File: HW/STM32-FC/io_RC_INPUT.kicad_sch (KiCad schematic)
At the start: 5 parts, among them J2 DSM, J4 RCIN, Q1 S9013

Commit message: 250102:STM32F407VET
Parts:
- added J9: RCIN, PWM_Connector:PWM_Conn_3x02, symbol PWM_Connector:PWM_Conn_3x01
- J4: symbol PWM_Connector:PWM_Conn_3x02 -> PWM_Connector:PWM_Conn_3x01
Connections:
- net +5V: now also J4.2 (5V), J9.2 (5V); no longer J4.3 (5V)
- net GND: now also J4.3 (GND), J9.3 (GND); no longer J4.4 (GND)
- net RSSI_IN: no longer J4.2 (CH2)
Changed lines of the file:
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@@
 		(color 0 0 0 0)
 	)
-	(junction
-		(at 49.53 48.26)
-		(diameter 0)
-		(color 0 0 0 0)
-	)
 	(wire
 		(pts
@@
 	(wire
 		(pts
+			(xy -20.32 60.96) (xy -11.43 60.96)
+		)
+		(stroke
+			(width 0)
+			(type default)
+		)
+	)
+	(wire
+		(pts
 			(xy 76.2 40.64) (xy 86.36 40.64)
 		)
@@
 	(wire
 		(pts
-			(xy 48.26 50.8) (xy 57.15 50.8)
-		)
-		(stroke
-			(width 0)
-			(type default)
-		)
-	)
-	(wire
-		(pts
 			(xy 55.88 105.41) (xy 54.61 105.41)
 		)
@@
 	(wire
 		(pts
-			(xy 49.53 63.5) (xy 52.07 63.5)
-		)
-		(stroke
-			(width 0)
-			(type default)
-		)
-	)
-	(wire
-		(pts
-			(xy 48.26 48.26) (xy 49.53 48.26)
-		)
-		(stroke
-			(width 0)
-			(type default)
-		)
-	)
-	(wire
-		(pts
 			(xy 76.2 38.1) (xy 76.2 40.64)
 		)
@@
 	(wire
 		(pts
+			(xy -36.83 54.61) (xy -35.56 54.61)
+		)
+		(stroke
+			(width 0)
+			(type default)
+		)
+	)
+	(wire
+		(pts
 			(xy 76.2 31.75) (xy 76.2 33.02)
 		)
@@
 	(wire
 		(pts
-			(xy 49.53 48.26) (xy 62.23 48.26)
-		)
-		(stroke
-			(width 0)
-			(type default)
-		)
-	)
-	(wire
-		(pts
-			(xy 49.53 48.26) (xy 49.53 63.5)
+			(xy -36.83 49.53) (xy -35.56 49.53)
+		)
+		(stroke
+			(width 0)
+			(type default)
+		)
+	)
+	(wire
+		(pts
+			(xy 48.26 48.26) (xy 62.23 48.26)
 		)
 		(stroke
@@
 		)
 	)
+	(label "RSSI_IN"
+		(at -11.43 60.96 180)
+		(fields_autoplaced yes)
+		(effects
+			(font
+				(size 1 1)
+			)
+			(justify right bottom)
+		)
+	)
 	(label "UART1_RX"
 		(at 60.96 139.7 180)
@@
 	(label "UART1_RX"
 		(at 63.5 110.49 180)
-		(fields_autoplaced yes)
-		(effects
-			(font
-				(size 1 1)
-			)
-			(justify right bottom)
-		)
-	)
-	(label "RSSI_IN"
-		(at 57.15 50.8 180)
 		(fields_autoplaced yes)
 		(effects
@@
 	)
 	(symbol
+		(lib_id "PWM_Connector:PWM_Conn_3x01")
+		(at -27.94 52.07 0)
+		(mirror y)
+		(unit 1)
+		(exclude_from_sim no)
+		(in_bom yes)
+		(on_board yes)
+		(dnp no)
+		(property "Reference" "J9"
+			(at -27.94 44.196 0)
+			(effects
+				(font
+					(size 1 1)
+				)
+			)
+		)
+		(property "Value" "RCIN"
+			(at -27.94 45.974 0)
+			(effects
+				(font
+					(size 1 1)
+				)
+			)
+		)
+		(property "Footprint" "PWM_Connector:PWM_Conn_3x02"
+			(at -36.83 55.88 0)
+			(effects
+				(font
+					(size 1.27 1.27)
+				)
+				(hide yes)
+			)
+		)
+		(property "Datasheet" "~"
+			(at -36.83 55.88 0)
+			(effects
+				(font
+					(size 1.27 1.27)
+				)
+				(hide yes)
+			)
+		)
+		(property "Description" "Generic connector, single row, 01x03, script generated (kicad-library-utils/schlib/autogen/connector/)"
+			(at -27.94 55.88 0)
+			(effects
+				(font
+					(size 1.27 1.27)
+				)
+				(hide yes)
+			)
+		)
+		(pin "1"
+		)
+		(pin "2"
+		)
+		(pin "3"
+		)
+		(instances
+			(project "STM32-FC"
+				(path "/8d4cc317-3933-4aa6-844b-8c5c635e89c7/77caf73d-b7f5-48a6-9de3-ef3df69ee7d9"
+					(reference "J9")
+					(unit 1)
+				)
+			)
+		)
+	)
+	(symbol
 		(lib_id "power:+3.3V")
 		(at 55.88 102.87 0)
@@
 	)
 	(symbol
+		(lib_id "power:+5V")
+		(at -36.83 49.53 90)
+		(unit 1)
+		(exclude_from_sim no)
+		(in_bom yes)
+		(on_board yes)
+		(dnp no)
+		(property "Reference" "#PWR059"
+			(at -33.02 49.53 0)
+			(effects
+				(font
+					(size 1.27 1.27)
+				)
+				(hide yes)
+			)
+		)
+		(property "Value" "+5V"
+			(at -38.354 47.752 90)
+			(effects
+				(font
+					(size 1 1)
+				)
+			)
+		)
+		(property "Footprint" ""
+			(at -36.83 49.53 0)
+			(effects
+				(font
+					(size 1.27 1.27)
+				)
+				(hide yes)
+			)
+		)
+		(property "Datasheet" ""
+			(at -36.83 49.53 0)
+			(effects
+				(font
+					(size 1.27 1.27)
+				)
+				(hide yes)
+			)
+		)
+		(property "Description" ""
+			(at -36.83 49.53 0)
+			(effects
+				(font
+					(size 1.27 1.27)
+				)
+				(hide yes)
+			)
+		)
+		(pin "1"
+		)
+		(instances
+			(project "STM32-FC"
+				(path "/8d4cc317-3933-4aa6-844b-8c5c635e89c7/77caf73d-b7f5-48a6-9de3-ef3df69ee7d9"
+					(reference "#PWR059")
+					(unit 1)
+				)
+			)
+		)
+	)
+	(symbol
+		(lib_id "power:GND")
+		(at -36.83 54.61 270)
+		(unit 1)
+		(exclude_from_sim no)
+		(in_bom yes)
+		(on_board yes)
+		(dnp no)
+		(property "Reference" "#PWR060"
+			(at -43.18 54.61 0)
+			(effects
+				(font
+					(size 1.27 1.27)
+				)
+				(hide yes)
+			)
+		)
+		(property "Value" "GND"
+			(at -38.1 57.15 90)
+			(effects
+				(font
+					(size 1 1)
+				)
+			)
+		)
+		(property "Footprint" ""
+			(at -36.83 54.61 0)
+			(effects
+				(font
+					(size 1.27 1.27)
+				)
+				(hide yes)
+			)
+		)
+		(property "Datasheet" ""
+			(at -36.83 54.61 0)
+			(effects
+				(font
+					(size 1.27 1.27)
+				)
+				(hide yes)
+			)
+		)
+		(property "Description" ""
+			(at -36.83 54.61 0)
+			(effects
+				(font
+					(size 1.27 1.27)
+				)
+				(hide yes)
+			)
+		)
+		(pin "1"
+		)
+		(instances
+			(project "STM32-FC"
+				(path "/8d4cc317-3933-4aa6-844b-8c5c635e89c7/77caf73d-b7f5-48a6-9de3-ef3df69ee7d9"
+					(reference "#PWR060")
+					(unit 1)
+				)
+			)
+		)
+	)
+	(symbol
 		(lib_id "power:GND")
 		(at 58.42 105.41 180)
@@
 	)
 	(symbol
-		(lib_id "PWM_Connector:PWM_Conn_3x02")
+		(lib_id "PWM_Connector:PWM_Conn_3x01")
 		(at 40.64 50.8 0)
 		(mirror y)
@@
 		(pin "3"
 		)
-		(pin "4"
-		)
-		(instances
+		(instances

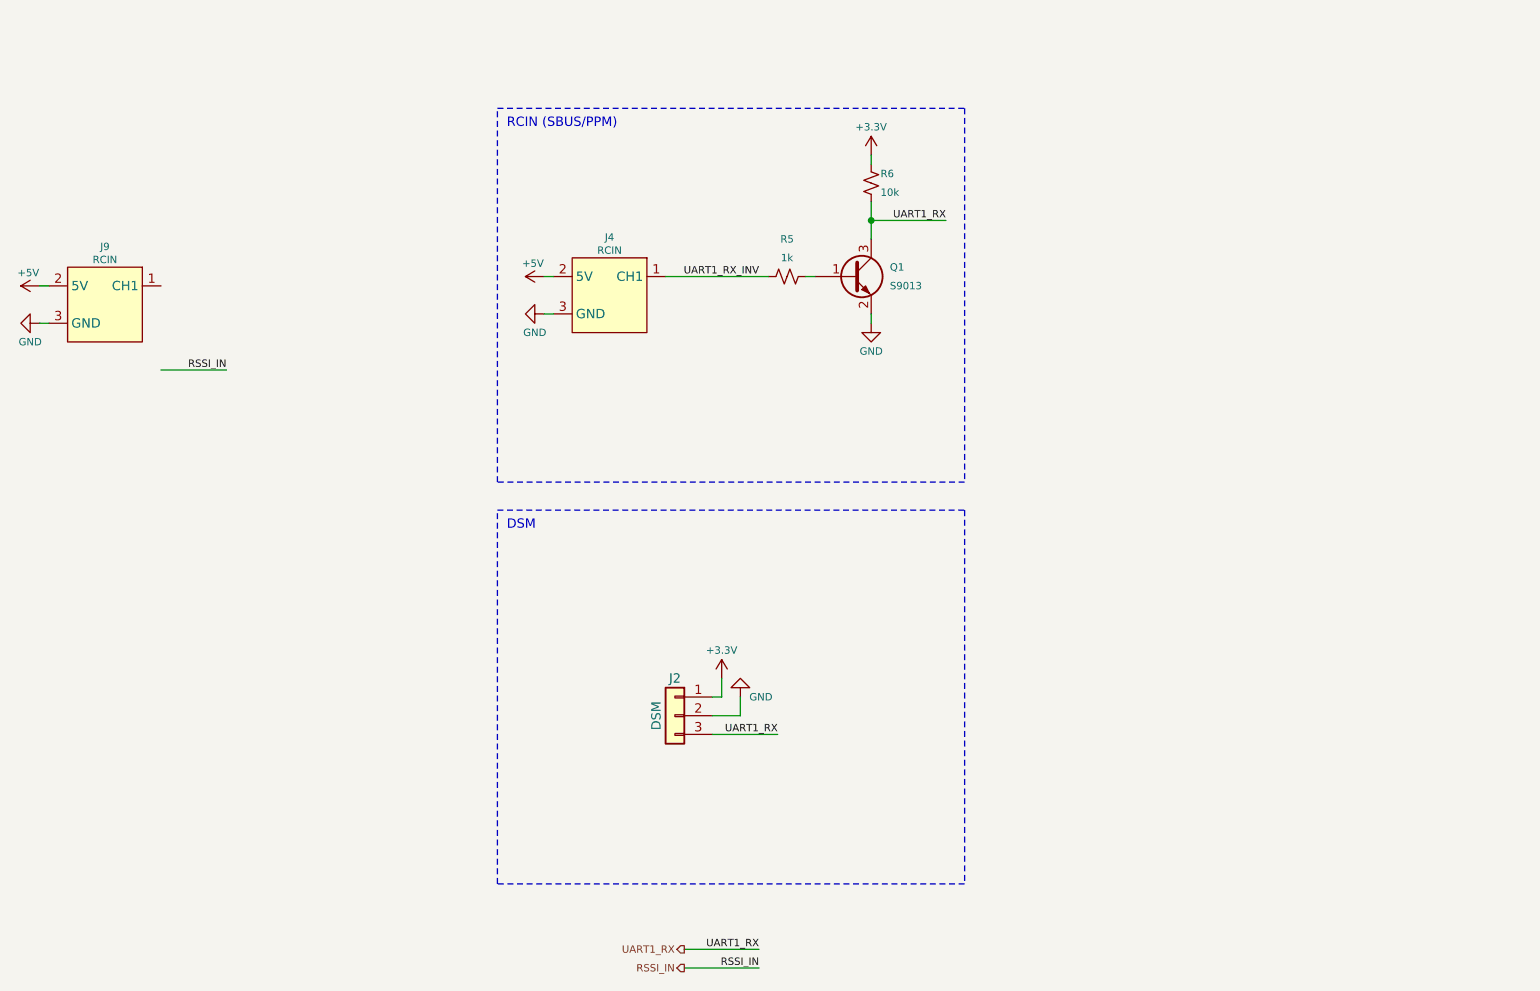
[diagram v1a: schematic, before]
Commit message: RC IN modified
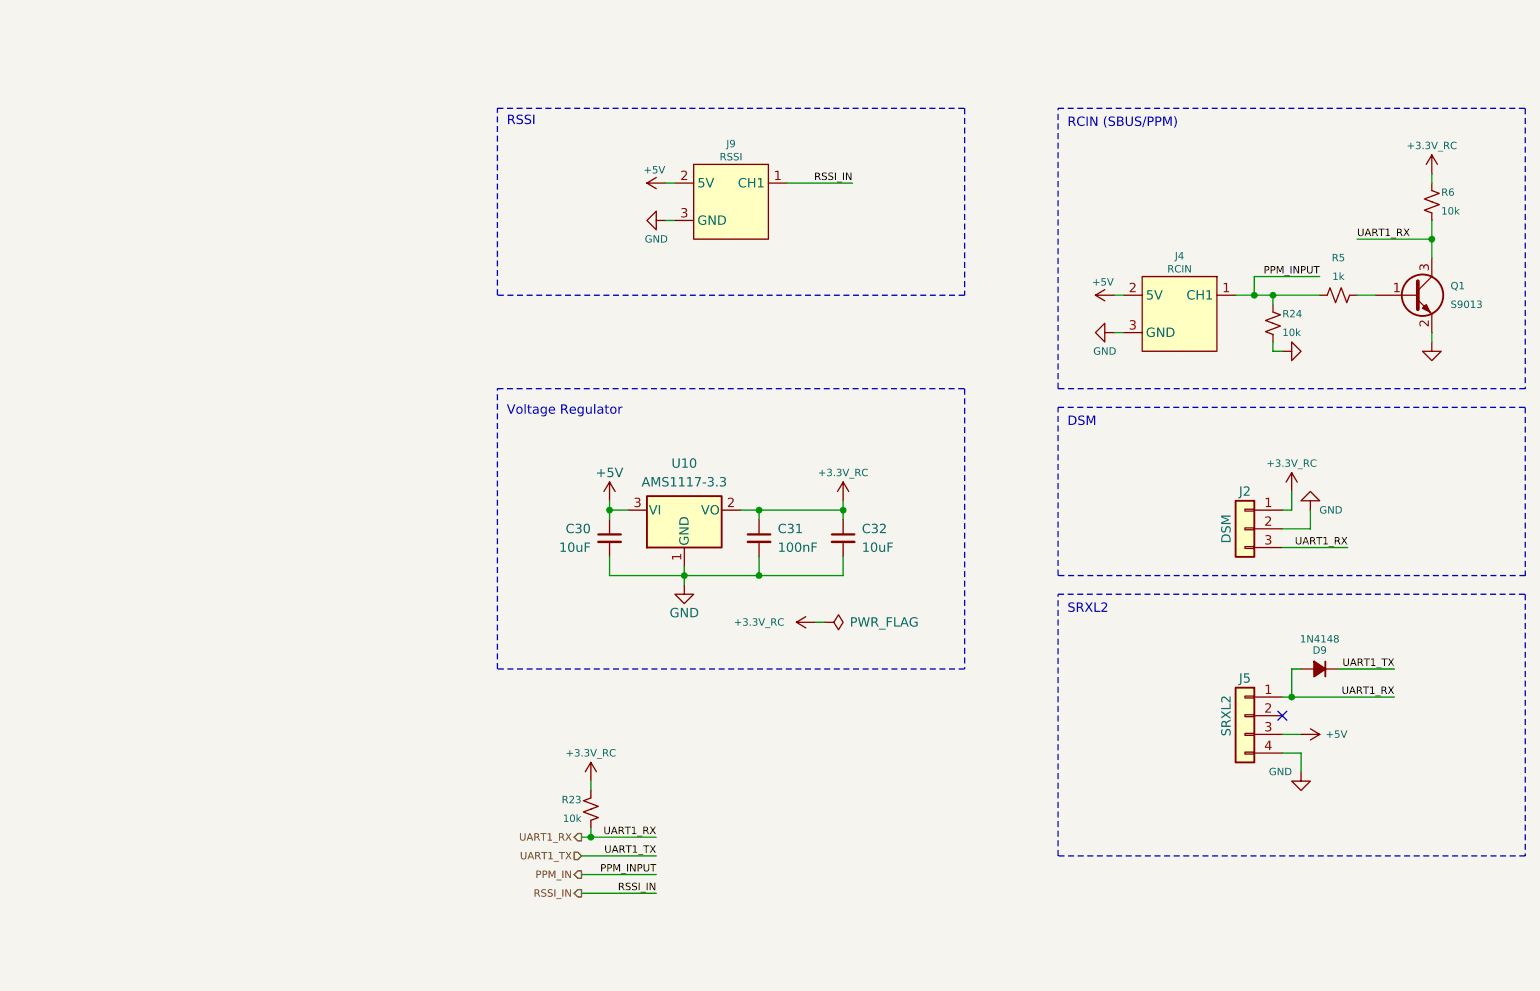
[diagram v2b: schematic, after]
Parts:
- added C30, C32: 10uF, Capacitor_SMD:C_0402_1005Metric, symbol Device:C_Small
- added C31: 100nF, Capacitor_SMD:C_0402_1005Metric, symbol Device:C_Small
- added D9: 1N4148, symbol Device:D_Small_Filled
- added J5: SRXL2, Connector_JST:JST_ZH_B3B-ZR-SM4-TF_1x03-1MP_P1.50mm_Vertical, symbol Connector_Generic:Conn_01x04
- added R23, R24: 10k, Resistor_SMD:R_0402_1005Metric, symbol Device:R_Small_US
- added U10: AMS1117-3.3, Package_TO_SOT_SMD:SOT-223-3_TabPin2, symbol Regulator_Linear:AMS1117-3.3
- J2: footprint Connector_PinHeader_2.54mm:PinHeader_1x03_P2.54mm_Vertical -> Connector_JST:JST_ZH_B3B-ZR-SM4-TF_1x03-1MP_P1.50mm_Vertical
- J9: value RCIN -> RSSI
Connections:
- net +5V: now also C30.1, J5.3 (Pin_3), U10.3 (VI)
- net GND: now also C30.2, C31.2, C32.2, J5.4 (Pin_4), R24.2, U10.1 (GND)
- net RSSI_IN: now also J9.1 (CH1)
- net UART1_RX: now also D9.2 (A), J5.1 (Pin_1), R23.2
- net +3.3V renamed +3.3V_RC
- net +3.3V_RC: now also C31.1, C32.1, R23.1, U10.2 (VO)
- net UART1_RX_INV renamed PPM_IN
- net PPM_IN: now also R24.1
- new net UART1_TX: D9.1 (K)
- no-connect marks 0 -> 1
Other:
- note added: "RSSI"
- note added: "SRXL2"
- note added: "Voltage Regulator"
- moved on the sheet: J2, J4, J9, Q1, R5, R6

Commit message: Big Update:IMU/RC/Conn./MCU
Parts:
- removed C30, C32: 10uF, Capacitor_SMD:C_0402_1005Metric, symbol Device:C_Small
- removed C31: 100nF, Capacitor_SMD:C_0402_1005Metric, symbol Device:C_Small
- removed U10: AMS1117-3.3, Package_TO_SOT_SMD:SOT-223-3_TabPin2, symbol Regulator_Linear:AMS1117-3.3
- D8: renamed from D9; footprint (none) -> Diode_SMD:D_SOD-123
- J7: renamed from J5; footprint Connector_JST:JST_ZH_B3B-ZR-SM4-TF_1x03-1MP_P1.50mm_Vertical -> Connector_JST:JST_ZH_B4B-ZR-SM4-TF_1x04-1MP_P1.50mm_Vertical
- Q2: renamed from Q1; footprint digikey-footprints:SOT-23-3 -> Package_TO_SOT_SMD:SOT-23-3
- renumbered J4 to J5, J2 to J6, J9 to J8, R24 to R12, R5 to R13, R6 to R14, R23 to R15
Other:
- note added: "2.54mm 3P PC0 : RSSI_IN"
- note added: "2.54mm 3P SBUS - PA10 : UART1_RX PPM - PB7 : TIM4_CH2"
- note added: "ZH 1.5mm 3P PA10 : UART1_RX"
- note added: "ZH 1.5mm 4P PA9 : UART1_TX PA10 : UART1_RX"
- note removed: "Voltage Regulator"
- company: (none) -> INHA UNIV. NARAE
- title: (none) -> RC_INPUT
- moved on the sheet: D8, J5, J6, J7, J8, Q2, R12, R13, R14, R15

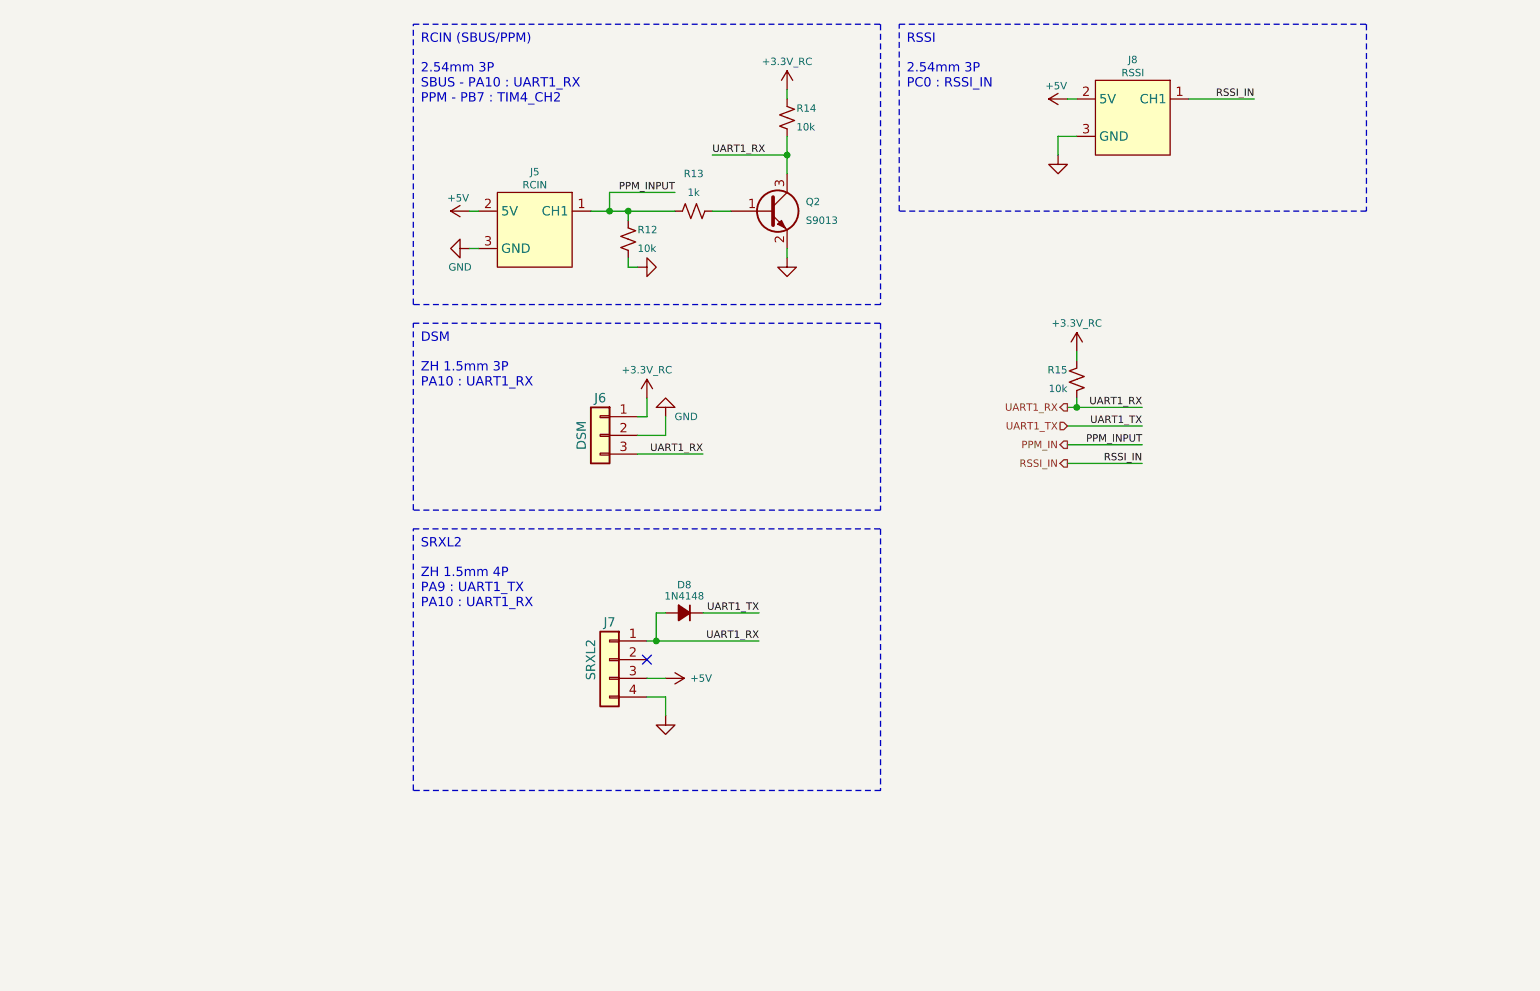
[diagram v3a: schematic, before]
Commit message: 2025.01.03v2:PM(Power Module) added
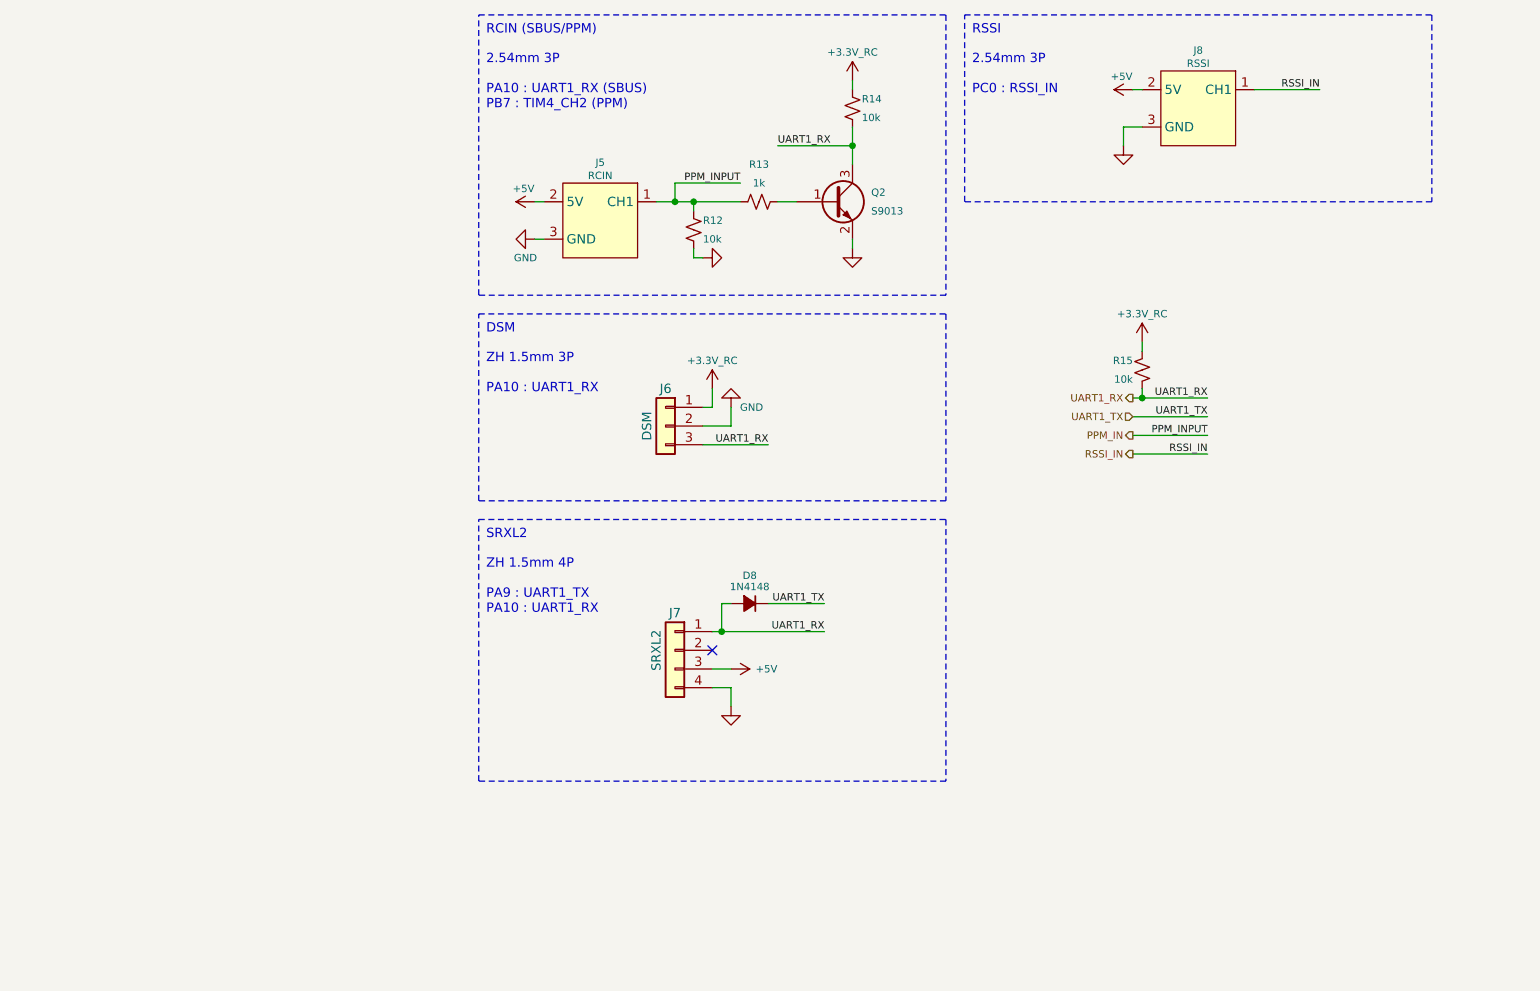
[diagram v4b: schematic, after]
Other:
- note added: "2.54mm 3P PA10 : UART1_RX (SBUS) PB7 : TIM4_CH2 (PPM)"
- note removed: "2.54mm 3P SBUS - PA10 : UART1_RX PPM - PB7 : TIM4_CH2"
- company: INHA UNIV. NARAE -> NARAE
- moved on the sheet: D8, J5, J6, J7, J8, Q2, R12, R13, R14, R15

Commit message: Baro/SD Card update
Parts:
- removed J5: RCIN, PWM_Connector:PWM_Conn_3x02, symbol PWM_Connector:PWM_Conn_3x01
- added J11: PWM_Conn_3x01, PWM_Connector:PWM_Conn_3x01, symbol PWM_Connector:PWM_Conn_3x01
- J10: renamed from J7; value SRXL2 -> ZH 1.5mm 4P; footprint Connector_JST:JST_ZH_B4B-ZR-SM4-TF_1x04-1MP_P1.50mm_Vertical -> Connector_JST:JST_ZH_S4B-ZR-SM4A-TF_1x04-1MP_P1.50mm_Horizontal
- J8: value RSSI -> PWM_Conn_3x01; footprint PWM_Connector:PWM_Conn_3x02 -> PWM_Connector:PWM_Conn_3x01
- J9: renamed from J6; value DSM -> ZH 1.5mm 3P; footprint Connector_JST:JST_ZH_B3B-ZR-SM4-TF_1x03-1MP_P1.50mm_Vertical -> Connector_JST:JST_ZH_S3B-ZR-SM4A-TF_1x03-1MP_P1.50mm_Horizontal
- renumbered D8 to D7, R12 to R18, R13 to R19, R14 to R20, R15 to R21
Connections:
- net +5V: now also J11.2 (5V)
- net GND: now also J11.3 (GND)
- net PPM_IN: now also J8.1 (CH1)
- net RSSI_IN: now also J11.1 (CH1); no longer J8.1 (CH1)
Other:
- note added: "2.54mm 3P PA10 : UART1_RX (SBUS) PD15 : TIM4_CH4 (PPM)"
- note removed: "2.54mm 3P PA10 : UART1_RX (SBUS) PB7 : TIM4_CH2 (PPM)"

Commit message: 2025.01.16
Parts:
- D7: footprint Diode_SMD:D_SOD-123 -> Diode_SMD:D_SOD-523
- renumbered J9 to J10, J10 to J11, J11 to J8, J8 to J9, R20 to R18, R18 to R20
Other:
- note added: "AUX1 : PB7 : TIM4_CH1 AUX2 : PE11 : TIM1_CH2 AUX3 : PE13 : TIM1_CH3 AUX4 : PE14 : TIM1_CH4"
- note added: "MAIN 1 : PA0 : TIM5_CH1 MAIN 2 : PA1 : TIM5_CH2 MAIN 3 : PA2 : TIM5_CH3 MAIN 4 : PA3 : TIM5_CH4 MAIN 5 : PC6 : TIM3_CH1 MAIN 6 : PC7 : TIM3_CH2 MAIN 7 : PB0 : TIM3_CH3 MAIN 8 : PB1 : TIM3_CH4"
- note added: "PWM RC OUT"
- moved on the sheet: R21
